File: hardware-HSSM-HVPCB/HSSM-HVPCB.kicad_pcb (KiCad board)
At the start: 4 copper layers, 42 x 29 mm, 71 parts, among them J2 805-108, K1 G6DN-1A-L DC12, K2 G6DN-1A-L DC12, Q1 Q_NMOS_SOT-23_IRLML6344, Q2 Q_NMOS_SOT-23_IRLML6344, U1 LNK3204D-TL, U2 CS5480-INZ, U3 LTV-354T, U4 LTV-354T, U5 LTV-354T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

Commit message: [#12] PCB Modify 860020372006 footprint
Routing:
- net AC_N: track 69.6 -> 68.6 mm

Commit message: [#12] PCB Routing WIP
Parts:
- moved R5 17.6 mm to (145.0, 107.0), turned to -90 degrees
- moved R6 14.4 mm to (143.7, 107.2), turned to 90 degrees
- moved Q1 10.9 mm to (141.1, 107.0), turned to 180 degrees
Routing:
- net AC_L: track 34.9 -> 44.8 mm, vias 4 -> 9
- net Net-(D5-A): track 2.51 -> 9.98 mm
- net /GPIO_S1: track 5.46 -> 10.4 mm, vias 2 -> 3
- net /GPIO_S3: track 0.00 -> 3.80 mm, vias 0 -> 1
- net +12V: track 30.3 -> 32.7 mm, vias 1 -> 2
- net /GPIO_Q1: track 0.00 -> 2.40 mm, vias 0 -> 1
- net /DO1: track 0.00 -> 2.40 mm, vias 0 -> 1
- net /DEV_TX: track 0.00 -> 2.40 mm, vias 0 -> 1
- net /GPIO_S2: track 3.10 -> 5.50 mm, vias 0 -> 1
- net unconnected-(CON1-Pad10): track 0.00 -> 1.97 mm, vias 0 -> 1
- net /GPIO_Q2: track 0.00 -> 1.97 mm, vias 0 -> 1
- net /DEV_RX: track 0.00 -> 1.97 mm, vias 0 -> 1
- net +3V3: track 11.0 -> 13.0 mm, vias 2 -> 3

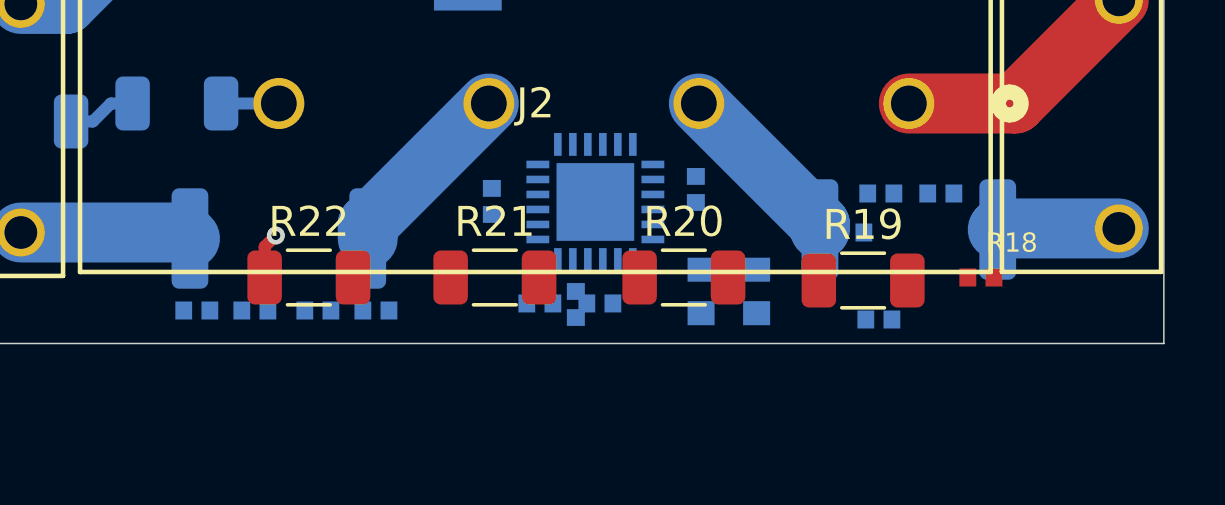
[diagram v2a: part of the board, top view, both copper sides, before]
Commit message: [#12] PCB Routing power measurement WIP
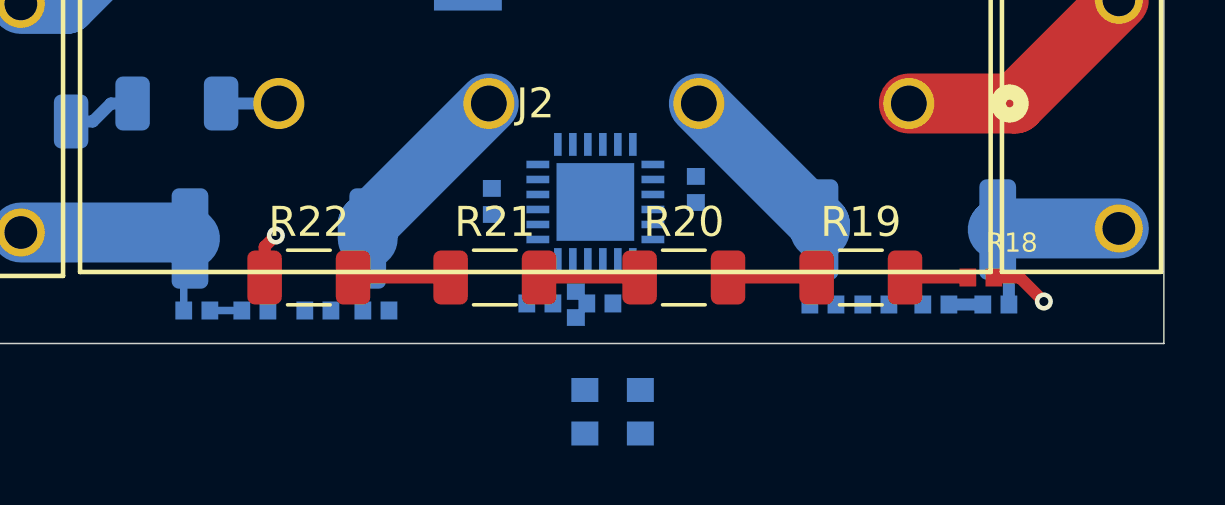
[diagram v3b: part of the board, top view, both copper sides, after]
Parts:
- moved Y1 5.58 mm to (155.1, 134.3)
- moved R27 5.40 mm to (167.9, 130.7), turned to 180 degrees
- moved C12 4.29 mm to (163.9, 130.7), turned to 0 degrees
- moved C11 4.13 mm to (165.9, 130.7), turned to 0 degrees
- moved R28 1.93 mm to (162.1, 130.7), turned to 0 degrees
- moved R19 0.13 mm to (163.4, 129.8)
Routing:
- net Net-(R20-Pad1): track 0.00 -> 3.35 mm
- net Net-(R21-Pad1): track 0.00 -> 3.25 mm
- net Net-(R19-Pad1): track 0.00 -> 2.95 mm
- net AC_Q2_SHNT2: track 4.05 -> 6.71 mm
- net AC_Q1_SHNT2: track 5.72 -> 8.21 mm
- net Net-(U2-VIN-): track 0.00 -> 2.09 mm
- net AC_L: track 44.8 -> 46.8 mm, vias 9 -> 10
- net Net-(U2-IIN2-): track 0.00 -> 1.13 mm
- net Net-(U2-IIN1-): track 0.00 -> 1.07 mm

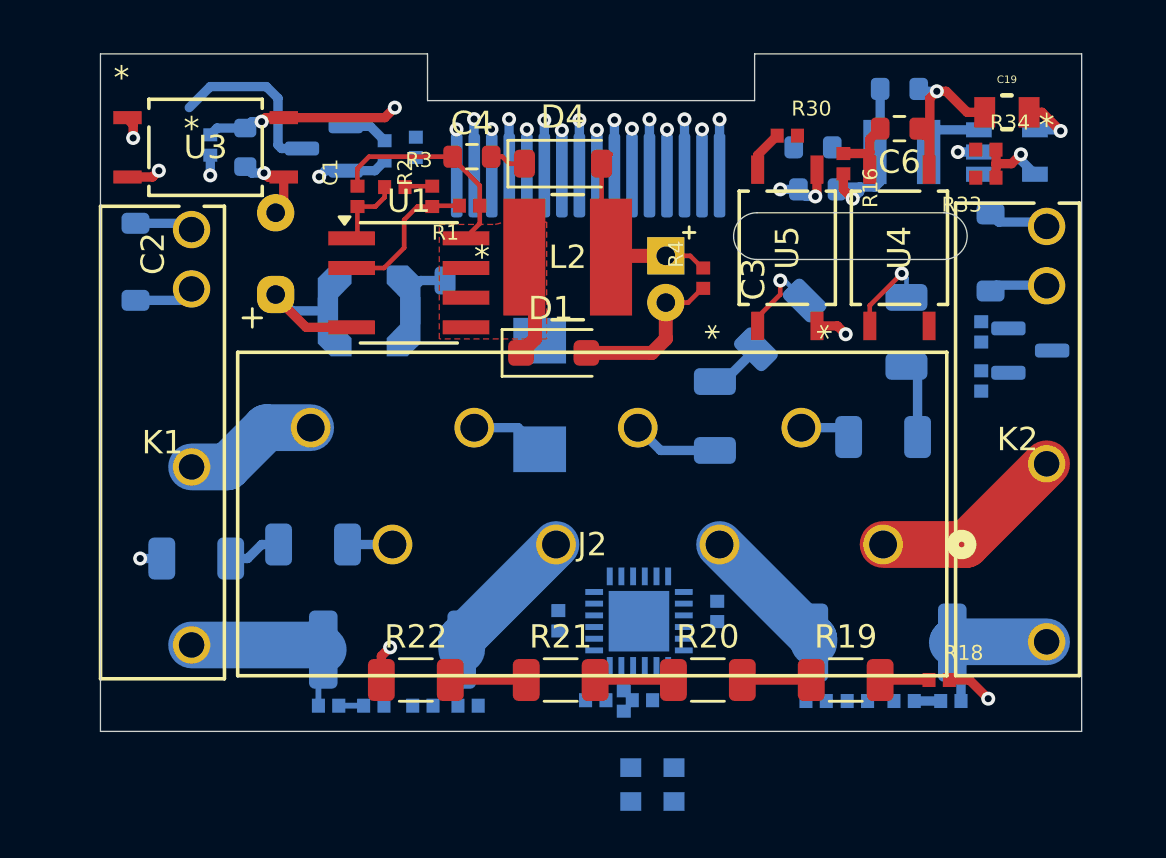
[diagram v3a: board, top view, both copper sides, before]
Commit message: [#12] PCB Routing  WIP swaped opto insulation HV inputs
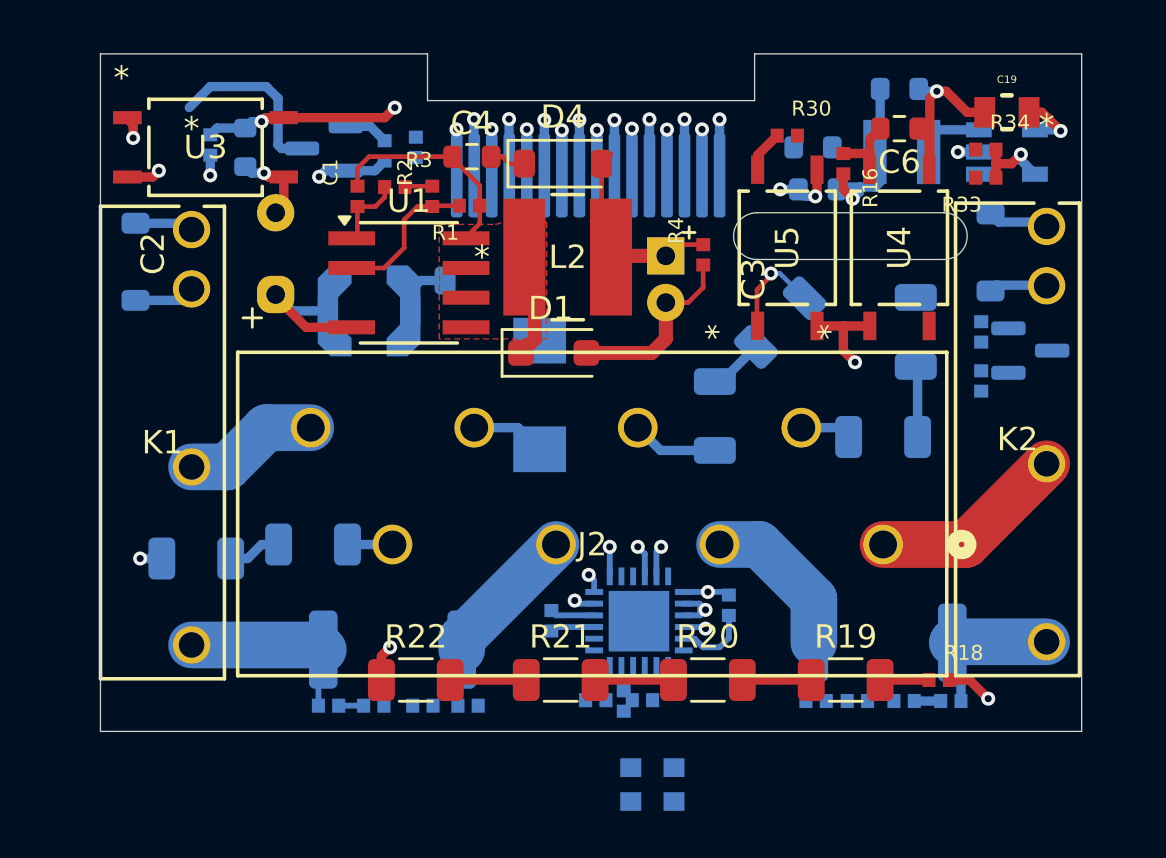
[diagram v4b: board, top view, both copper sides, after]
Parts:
- moved R4 1.00 mm to (157.3, 111.6)
- moved C14 0.57 mm to (158.4, 126.6)
- moved R15 0.40 mm to (166.4, 114.9)
- moved C13 0.30 mm to (150.8, 127.3)
- moved R29 0.10 mm to (160.6, 114.5)
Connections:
- R15 pad 2: Net-(U4-A) -> Net-(U4-K)
- U4 pad 1: Net-(U4-A) -> AC_N
- U4 pad 2: AC_N -> Net-(U4-K)
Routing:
- net /DEV_TX: track 2.40 -> 54.1 mm, vias 1 -> 2
- net /DEV_RX: track 1.97 -> 50.7 mm, vias 1 -> 2
- net AC_L: track 46.8 -> 52.6 mm, vias 10 -> 13
- net Net-(U4-A): track 3.92 -> 0.00 mm, vias 1 -> 0
- net +3V3: track 13.0 -> 16.4 mm, vias 3 -> 5
- net Net-(U2-VDDD): track 0.00 -> 3.22 mm
- net AC_N: track 68.6 -> 66.1 mm
- net Net-(U2-VREF+): track 0.00 -> 1.92 mm
- net Net-(U2-VREF-): track 0.00 -> 1.90 mm
- net /DO1: track 2.40 -> 3.66 mm, vias 1 -> 2
- net Net-(U5-A): track 3.77 -> 4.39 mm

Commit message: [#12] PCB Routing WIP S1
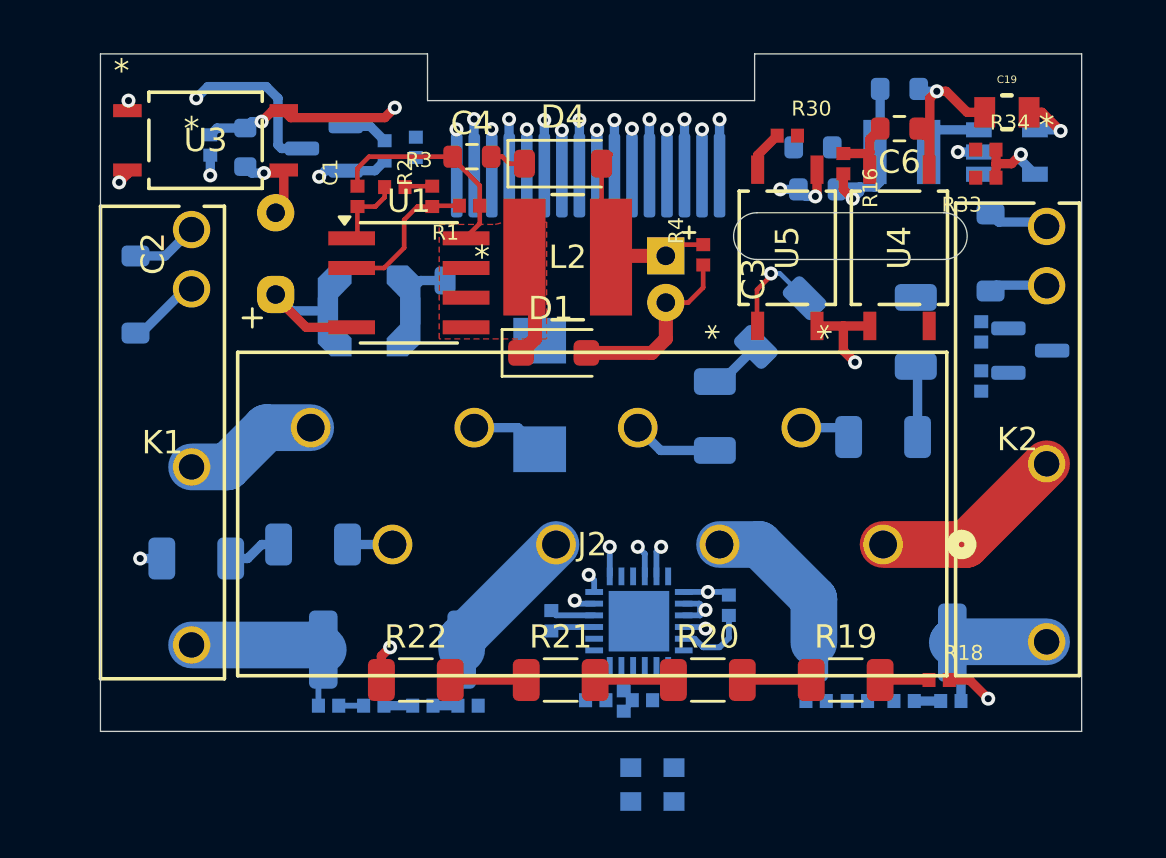
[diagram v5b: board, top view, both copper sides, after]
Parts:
- moved D5 1.40 mm to (133.0, 113.3)
- moved U3 0.30 mm to (136.0, 106.7)
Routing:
- net Net-(D5-A): track 9.98 -> 15.6 mm, vias 0 -> 1
- net Net-(U3-A): track 20.5 -> 23.0 mm
- net AC_N: track 66.1 -> 63.7 mm
- net +12V: track 32.7 -> 34.8 mm
- net AC_L: track 52.6 -> 54.1 mm
- net Net-(U2-IIN1+): track 0.00 -> 1.07 mm

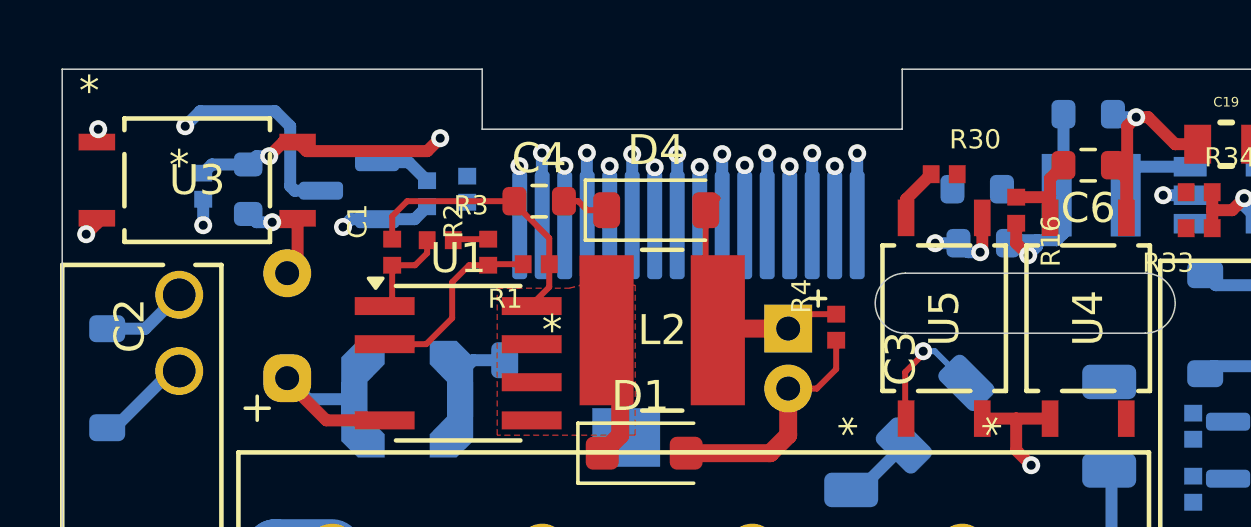
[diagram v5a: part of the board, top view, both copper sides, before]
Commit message: [#12] PCB Routing WIP DCDC converter
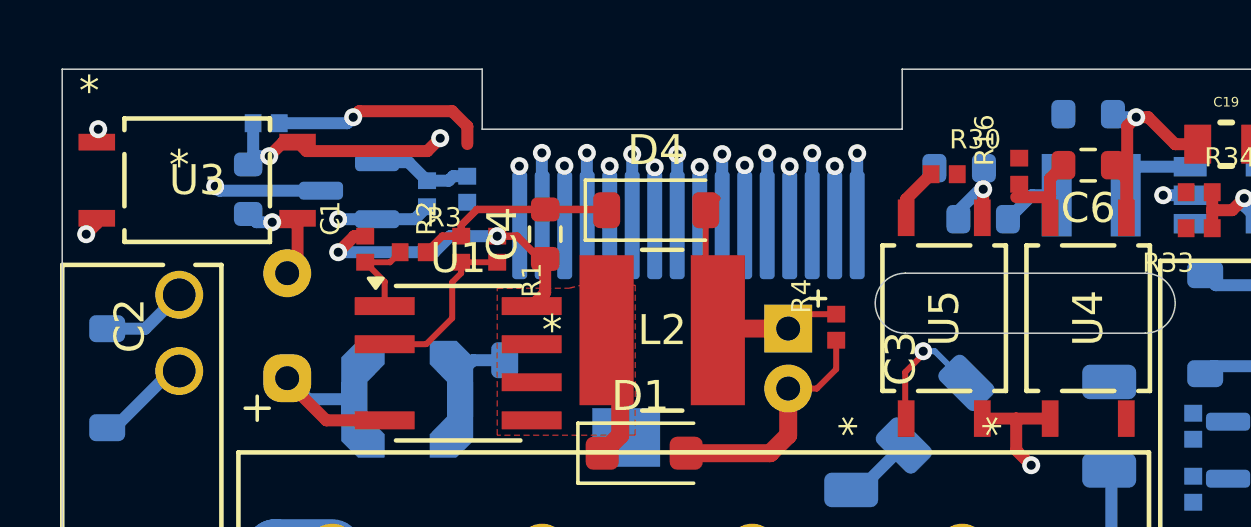
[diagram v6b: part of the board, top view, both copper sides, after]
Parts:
- moved R13 2.97 mm to (138.3, 104.8), turned to 0 degrees
- moved R1 1.39 mm to (146.0, 109.0), turned to -90 degrees
- moved R16 1.30 mm to (163.4, 106.4), turned to 90 degrees
- moved C4 1.12 mm to (147.6, 108.5), turned to 90 degrees
- moved R3 0.98 mm to (143.2, 109.1)
- moved C16 0.92 mm to (161.4, 106.3)
- moved C1 0.91 mm to (141.6, 109.0)
- moved R2 0.91 mm to (144.8, 109.0)
- moved C18 0.80 mm to (162.2, 108.0)
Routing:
- net Net-(D5-A): track 15.6 -> 10.6 mm
- net Net-(D4-K): track 2.73 -> 6.83 mm
- net +3V3: track 16.4 -> 14.6 mm, vias 5 -> 4
- net Net-(Q1-G): track 1.92 -> 3.32 mm
- net Net-(D1-K): track 13.8 -> 14.9 mm, vias 0 -> 2
- net Net-(U1-FB): track 6.42 -> 5.78 mm
- net AC_L: track 54.1 -> 53.8 mm, vias 13 -> 12

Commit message: [#12] PCB Routing WIP
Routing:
- net +12V: track 34.8 -> 90.2 mm
- net /GPIO_S2: track 5.50 -> 10.9 mm
- net +3V3: track 14.6 -> 18.0 mm, vias 4 -> 6
- net /GPIO_S3: track 3.80 -> 5.88 mm, vias 1 -> 2
- net /DEV_TX: track 53.7 -> 54.3 mm, vias 2 -> 4
- net /DEV_RX: track 51.0 -> 51.6 mm, vias 2 -> 4
- net AC_L: track 53.8 -> 53.3 mm, vias 12 -> 14
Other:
- outline, holes or cut-outs redrawn

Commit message: [#12] PCB Routing WIP
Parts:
- C19: moved to B.Cu
- Q2, R7, R8: moved to F.Cu
- moved R7 12.5 mm to (169.1, 104.5), turned to 180 degrees
- moved R8 10.6 mm to (171.6, 104.6), turned to 0 degrees
- moved Q2 8.57 mm to (171.7, 107.1), turned to -90 degrees
- moved C19 1.24 mm to (170.6, 104.3)
- moved R30 1.03 mm to (161.8, 106.0)
- moved R34 0.51 mm to (168.9, 107.0)
- moved R33 0.50 mm to (168.9, 108.3)
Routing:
- net /GPIO_Q2: track 1.97 -> 17.1 mm
- net AC_L: track 53.3 -> 59.5 mm
- net Net-(Q2-G): track 0.00 -> 5.23 mm
- net /GPIO_S2: track 10.9 -> 14.5 mm
- net +3V3: track 18.0 -> 21.5 mm
- net /GPIO_S3: track 5.88 -> 9.32 mm
- net Net-(U4-K): track 0.00 -> 2.92 mm, vias 0 -> 1
- net /DEV_RX: track 51.6 -> 52.5 mm
- net /DEV_TX: track 54.3 -> 54.9 mm
- removed copper zone on In2.Cu, net +12V
